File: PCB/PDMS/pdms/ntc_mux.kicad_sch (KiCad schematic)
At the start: 4 parts

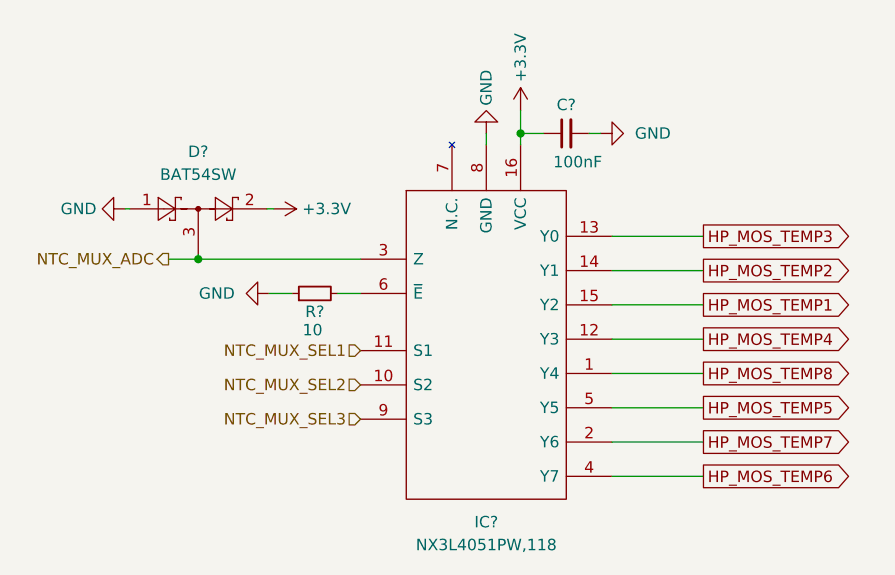
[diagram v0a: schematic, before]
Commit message: PCB - Low power mosf voltage mux
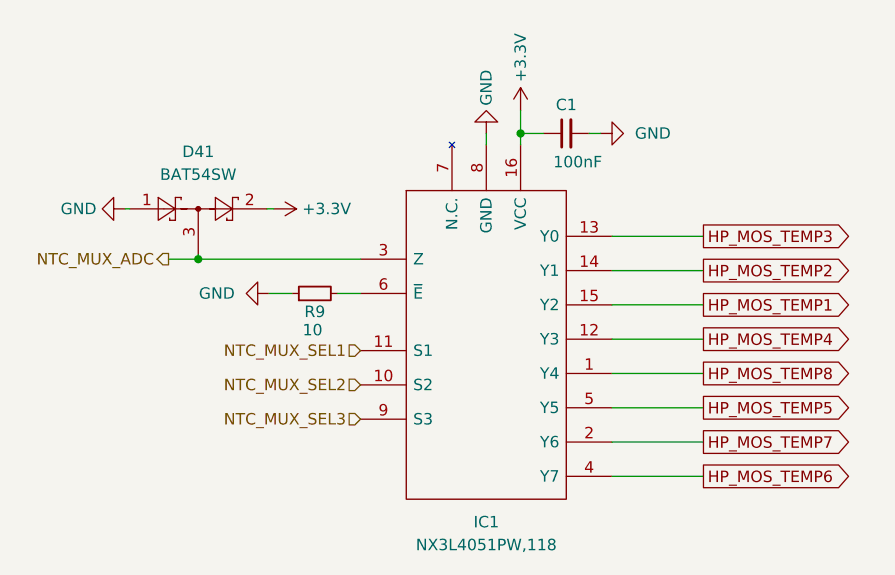
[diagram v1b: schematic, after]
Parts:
- gave numbers to parts that had none: 4
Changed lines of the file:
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@@
   (symbol (lib_id "power:GND") (at 85.852 68.072 270) (unit 1)
     (in_bom yes) (on_board yes) (fields_autoplaced)
-    (property "Reference" "#PWR?" (id 0) (at 79.502 68.072 0)
+    (property "Reference" "#PWR0124" (id 0) (at 79.502 68.072 0)
       (effects (font (size 1.27 1.27)) hide)
     )
@@
   (symbol (lib_id "power:+3.3V") (at 129.794 57.15 0) (unit 1)
     (in_bom yes) (on_board yes)
-    (property "Reference" "#PWR?" (id 0) (at 129.794 60.96 0)
+    (property "Reference" "#PWR0123" (id 0) (at 129.794 60.96 0)
       (effects (font (size 1.27 1.27)) hide)
     )
@@
   (symbol (lib_id "Device:R_Small") (at 106.934 77.47 90) (unit 1)
     (in_bom yes) (on_board yes)
-    (property "Reference" "R?" (id 0) (at 106.934 79.502 90))
+    (property "Reference" "R9" (id 0) (at 106.934 79.502 90))
     (property "Value" "10" (id 1) (at 106.68 81.534 90))
     (property "Footprint" "Resistor_SMD:R_0402_1005Metric" (id 2) (at 106.934 77.47 0)
@@
   (symbol (lib_id "power:GND") (at 125.984 59.69 180) (unit 1)
     (in_bom yes) (on_board yes)
-    (property "Reference" "#PWR?" (id 0) (at 125.984 53.34 0)
+    (property "Reference" "#PWR0122" (id 0) (at 125.984 53.34 0)
       (effects (font (size 1.27 1.27)) hide)
     )
@@
   (symbol (lib_id "power:+3.3V") (at 102.362 68.072 270) (unit 1)
     (in_bom yes) (on_board yes) (fields_autoplaced)
-    (property "Reference" "#PWR?" (id 0) (at 98.552 68.072 0)
+    (property "Reference" "#PWR0136" (id 0) (at 98.552 68.072 0)
       (effects (font (size 1.27 1.27)) hide)
     )
@@
   (symbol (lib_id "Device:C_Small") (at 134.874 59.69 90) (unit 1)
     (in_bom yes) (on_board yes)
-    (property "Reference" "C?" (id 0) (at 134.874 56.515 90))
+    (property "Reference" "C1" (id 0) (at 134.874 56.515 90))
     (property "Value" "100nF" (id 1) (at 136.144 62.865 90))
     (property "Footprint" "Capacitor_SMD:C_0402_1005Metric" (id 2) (at 134.874 59.69 0)
@@
   (symbol (lib_id "power:GND") (at 138.684 59.69 90) (unit 1)
     (in_bom yes) (on_board yes) (fields_autoplaced)
-    (property "Reference" "#PWR?" (id 0) (at 145.034 59.69 0)
+    (property "Reference" "#PWR0137" (id 0) (at 145.034 59.69 0)
       (effects (font (size 1.27 1.27)) hide)
     )
@@
   (symbol (lib_id "power:GND") (at 101.854 77.47 270) (unit 1)
     (in_bom yes) (on_board yes) (fields_autoplaced)
-    (property "Reference" "#PWR?" (id 0) (at 95.504 77.47 0)
+    (property "Reference" "#PWR0134" (id 0) (at 95.504 77.47 0)
       (effects (font (size 1.27 1.27)) hide)
     )
@@
   (symbol (lib_id "Diode:BAT54SW") (at 93.98 68.072 0) (unit 1)
     (in_bom yes) (on_board yes) (fields_autoplaced)
-    (property "Reference" "D?" (id 0) (at 93.98 61.722 0))
+    (property "Reference" "D41" (id 0) (at 93.98 61.722 0))
     (property "Value" "BAT54SW" (id 1) (at 93.98 64.262 0))
     (property "Footprint" "Package_TO_SOT_SMD:SOT-323_SC-70" (id 2) (at 95.885 64.897 0)
@@
   (symbol (lib_id "pdms_additional:NX3L4051PW,118") (at 112.014 68.58 0) (unit 1)
     (in_bom yes) (on_board yes) (fields_autoplaced)
-    (property "Reference" "IC?" (id 0) (at 125.984 102.87 0))
+    (property "Reference" "IC1" (id 0) (at 125.984 102.87 0))
     (property "Value" "NX3L4051PW,118" (id 1) (at 125.984 105.41 0))
     (property "Footprint" "PDMS_Additional:SOP65P640X110-16N" (id 2) (at 171.704 60.96 0)
